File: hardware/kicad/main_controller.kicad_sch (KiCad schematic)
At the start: 24 parts, among them J3 JTAG_10PIN, SW1 RESET, SW2 BOOT, U6 ESP32-S3-MINI-1, Y1 32.768 kHz

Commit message: PCB Layout Update
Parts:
- added D5: ESDA6V1W5, Package_TO_SOT_SMD:SOT-353_SC-70-5, symbol Power_Protection:SP0504BAJT
- added D9 (x2): ESD5651N, Capacitor_SMD:C_0402_1005Metric, symbol Device:D_TVS
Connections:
- net ESP_EN is gone; now on net CHIP_EN: U6.45 (EN)
- net +3V3: now also D9.2 (A2)
- net CELL_EN: now also U6.18 (GPIO14/TOUCH14/ADC2_CH3/FSPIWP/FSPIDQS/SUBSPIWP); no longer U6.30 (GPIO48/SPICLK_N/SUBSPICLK_N_DIFF)
- net CELL_PWRKEY: now also U6.13 (GPIO9/TOUCH9/ADC1_CH8/FSPIHD/SUBSPIHD); no longer U6.27 (GPIO47/SPICLK_P/SUBSPICLK_P_DIFF)
- net CELL_RESET: now also U6.16 (GPIO12/TOUCH12/ADC2_CH1/FSPICLK/FSPIIO6/SUBSPICLK); no longer U6.29 (SPIIO5/GPIO34/FSPICS0/SUBSPICS0)
- net CELL_RXD: now also U6.15 (GPIO11/TOUCH11/ADC2_CH0/FSPID/FSPIIO5/SUBSPID); no longer U6.21 (GPIO17/U1TXD/ADC2_CH6)
- net CELL_STATUS: now also U6.21 (GPIO17/U1TXD/ADC2_CH6); no longer U6.28 (SPIIO4/GPIO33/FSPIHD/SUBSPIHD)
- net CELL_TXD: now also U6.14 (GPIO10/TOUCH10/ADC1_CH9/FSPICS0/FSPIIO4/SUBSPICS0); no longer U6.22 (GPIO18/U1RXD/ADC2_CH7/CLK_OUT3)
- net CHIP_EN: now also D9.2 (A2)
- net FG_INT: now also U6.22 (GPIO18/U1RXD/ADC2_CH7/CLK_OUT3); no longer U6.25 (GPIO21)
- net GND: now also D5.2 (A), D9.1 (A1), D9.1 (A1)
- net GNSS_EN: now also U6.9 (GPIO5/TOUCH5/ADC1_CH4); no longer U6.5 (GPIO1/TOUCH1/ADC1_CH0)
- net GNSS_FO: now also U6.8 (GPIO4/TOUCH4/ADC1_CH3); no longer U6.33 (SPIDQS/GPIO37/FSPIQ/SUBSPIQ)
- net GNSS_RESET: now also U6.5 (GPIO1/TOUCH1/ADC1_CH0); no longer U6.34 (GPIO38/FSPIWP/SUBSPIWP)
- net GNSS_RXD: now also U6.10 (GPIO6/TOUCH6/ADC1_CH5); no longer U6.31 (SPIIO6/GPIO35/FSPID/SUBSPID)
- net GNSS_SDBY: now also U6.6 (GPIO2/TOUCH2/ADC1_CH1); no longer U6.41 (GPIO45)
- net GNSS_TXD: now also U6.11 (GPIO7/TOUCH7/ADC1_CH6); no longer U6.32 (SPIIO7/GPIO36/FSPICLK/SUBSPICLK)
- net GNSS_VBCKP_EN: now also U6.12 (GPIO8/TOUCH8/ADC1_CH7/SUBSPICS1); no longer U6.26 (GPIO26)
- net IMU_INT: now also U6.17 (GPIO13/TOUCH13/ADC2_CH2/FSPIQ/FSPIIO7/SUBSPIQ); no longer U6.6 (GPIO2/TOUCH2/ADC1_CH1)
- net JTAG_TCK: now also D5.3 (K)
- net JTAG_TDI: now also D5.4 (K)
- net JTAG_TDO: now also D5.1 (K)
- net JTAG_TMS: now also D5.5 (K)
- net SCL: now also U6.32 (SPIIO7/GPIO36/FSPICLK/SUBSPICLK); no longer U6.16 (GPIO12/TOUCH12/ADC2_CH1/FSPICLK/FSPIIO6/SUBSPICLK)
- net SDA: now also U6.33 (SPIDQS/GPIO37/FSPIQ/SUBSPIQ); no longer U6.17 (GPIO13/TOUCH13/ADC2_CH2/FSPIQ/FSPIIO7/SUBSPIQ)
- no-connect marks 11 -> 4
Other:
- note added: "ESP32-S3-MINI-N4R2"
- note added: "Octal SPI"
- note added: "internal flash/PSRAM"
- note added: "strapping pin"
- moved on the sheet: C15, C16, J3, R11, R15, R18, R7, R8, R9, TP7, TP8, Y1

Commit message: PCB Layout Update
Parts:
- added D1: Yellow, LED_SMD:LED_0603_1608Metric, symbol Device:LED_Small
- added D1: Green, LED_SMD:LED_0603_1608Metric, symbol Device:LED_Small
- added R5 (x2): 1k, Resistor_SMD:R_0402_1005Metric, symbol Device:R_Small
- added TP7: GPIO38, TestPoint:TestPoint_Pad_D1.0mm, symbol Connector:TestPoint
- added TP7: GPIO45, TestPoint:TestPoint_Pad_D1.0mm, symbol Connector:TestPoint
- added TP7: GPIO35, TestPoint:TestPoint_Pad_D1.0mm, symbol Connector:TestPoint
- added TP7: GPIO03, TestPoint:TestPoint_Pad_D1.0mm, symbol Connector:TestPoint
- added TP7: GPIO21, TestPoint:TestPoint_Pad_D1.0mm, symbol Connector:TestPoint
- added TP7: GPIO34, TestPoint:TestPoint_Pad_D1.0mm, symbol Connector:TestPoint
- added TP7: GPIO33, TestPoint:TestPoint_Pad_D1.0mm, symbol Connector:TestPoint
- added TP7: GPIO46, TestPoint:TestPoint_Pad_D1.0mm, symbol Connector:TestPoint
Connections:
- net GND: now also R5.2, R5.2
- net at U6.25 (GPIO21): now also TP7.1
- net at U6.27 (GPIO47/SPICLK_P/SUBSPICLK_P_DIFF): now also D1.2 (A)
- net at U6.28 (SPIIO4/GPIO33/FSPIHD/SUBSPIHD): now also TP7.1
- net at U6.29 (SPIIO5/GPIO34/FSPICS0/SUBSPICS0): now also TP7.1
- net at U6.30 (GPIO48/SPICLK_N/SUBSPICLK_N_DIFF): now also D1.2 (A)
- net at U6.31 (SPIIO6/GPIO35/FSPID/SUBSPID): now also TP7.1
- net at U6.34 (GPIO38/FSPIWP/SUBSPIWP): now also TP7.1
- net at U6.41 (GPIO45): now also TP7.1
- net at U6.7 (GPIO3/TOUCH3/ADC1_CH2): now also TP7.1
- net BOOT_MODE1: no longer names the net of U6.44 (GPIO46)
- net BOOT_MODE1: now also TP7.1
- new net: D1.1 (K), R5.1 (x2)
- no-connect marks 4 -> 2
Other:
- note added: "ESP32-S3-MINI-N4R2 (Quad SPI)"
- note removed: "ESP32-S3-MINI-N4R2"
- moved on the sheet: R9

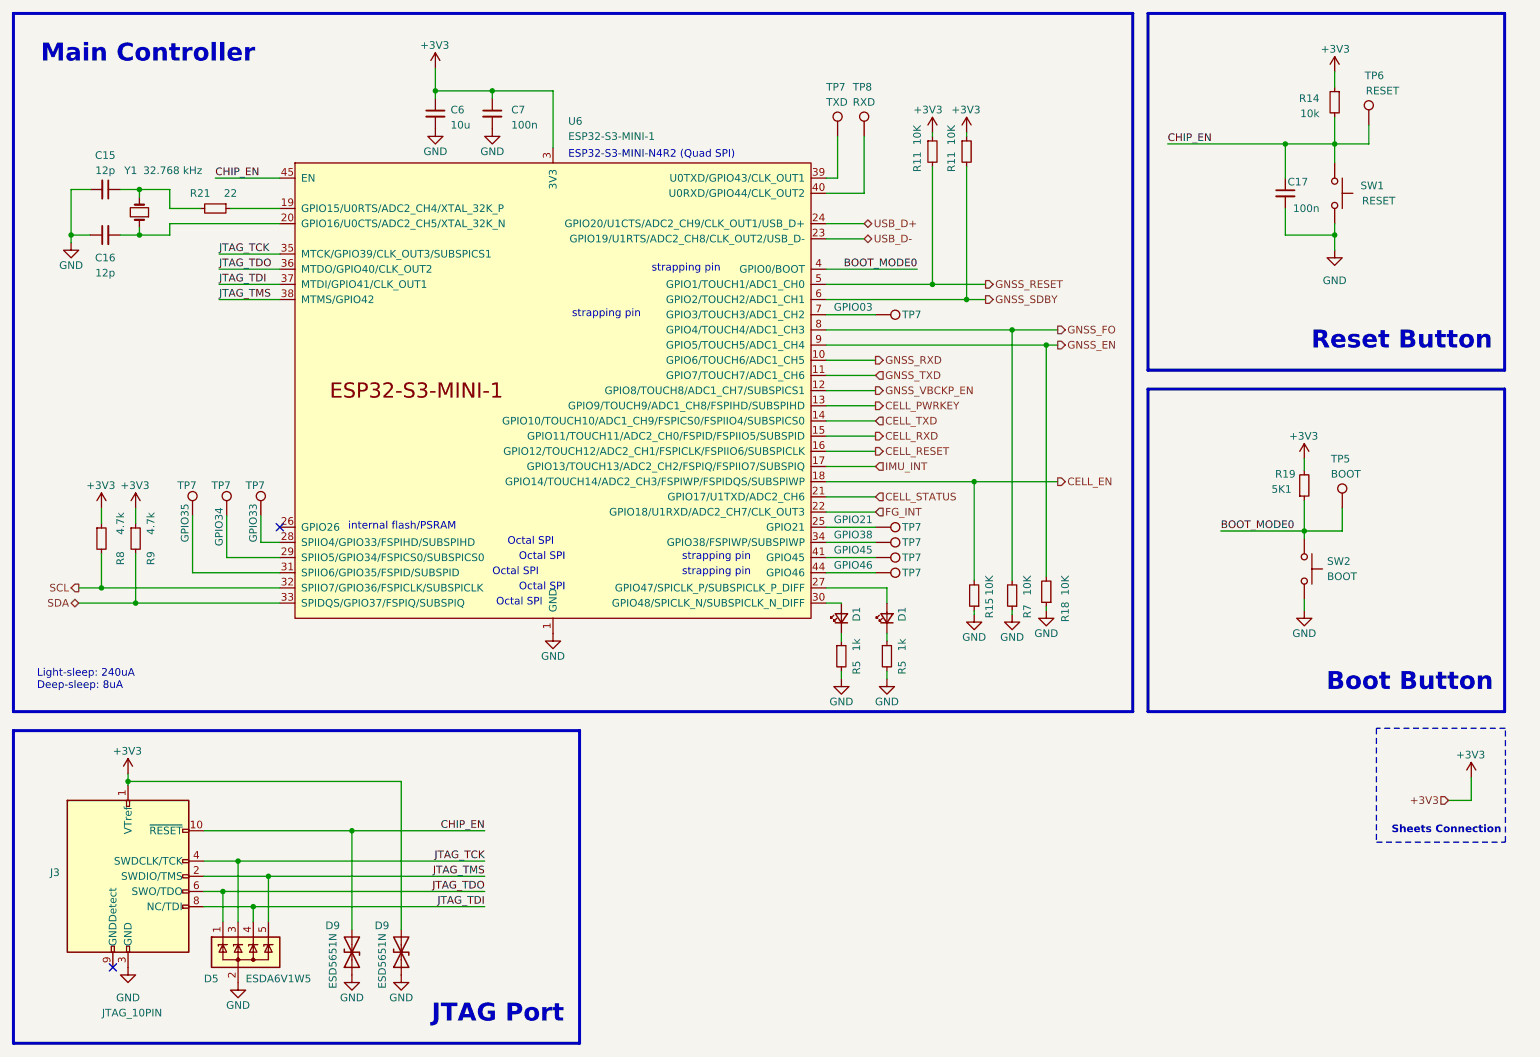
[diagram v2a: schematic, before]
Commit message: update to KiCAD 8 and add cell power regulator
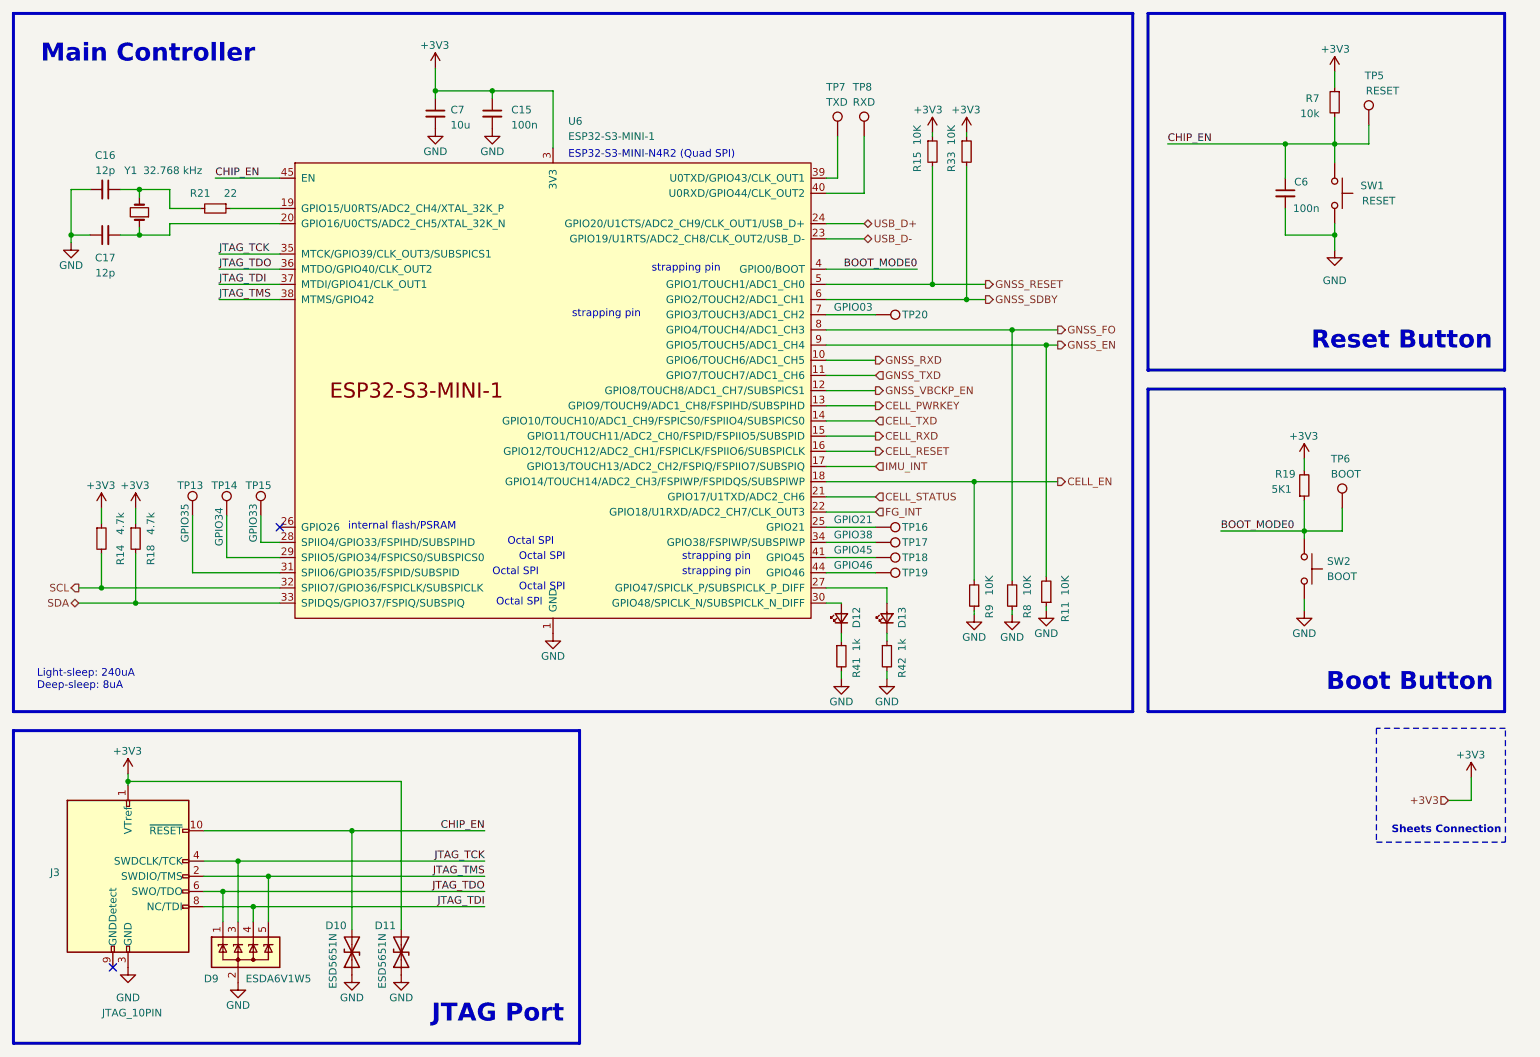
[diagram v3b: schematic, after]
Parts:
- renumbered C7 to C15, C15 to C16, C16 to C17, C17 to C6, C6 to C7, D9 to D10, D9 to D11, D1 to D12, D1 to D13, D5 to D9, R18 to R11, R8 to R14, R11 to R15, R9 to R18, R11 to R33, R5 to R41, R5 to R42, R14 to R7, R7 to R8, R15 to R9, TP7 to TP13, TP7 to TP14, TP7 to TP15, TP7 to TP16, TP7 to TP17, TP7 to TP18, TP7 to TP19, TP7 to TP20, TP6 to TP5, TP5 to TP6

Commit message: move components to use bwlc1a library
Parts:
- SW1, SW2: footprint Button_Switch_SMD:SW_Push_1P1T_NO_CK_KMR2 -> bwlc1a:SW-SMD_L3.9-W3.0-P4.45
- U6: footprint Espressif:ESP32-S3-MINI-1 -> bwlc1a:ESP32-S3-MINI-1; symbol Espressif:ESP32-S3-MINI-1 -> bwlc1a:ESP32-S3-MINI-1
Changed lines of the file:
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@@
 			)
 		)
-		(property "Footprint" "Button_Switch_SMD:SW_Push_1P1T_NO_CK_KMR2"
+		(property "Footprint" "bwlc1a:SW-SMD_L3.9-W3.0-P4.45"
 			(at 245.11 113.03 0)
 			(effects
@@
 	)
 	(symbol
-		(lib_id "Espressif:ESP32-S3-MINI-1")
+		(lib_id "bwlc1a:ESP32-S3-MINI-1")
 		(at 114.3 83.185 0)
 		(unit 1)
@@
 			)
 		)
-		(property "Footprint" "Espressif:ESP32-S3-MINI-1"
+		(property "Footprint" "bwlc1a:ESP32-S3-MINI-1"
 			(at 114.3 139.065 0)
 			(effects
@@
 			)
 		)
-		(property "Description" "SMD WiFi Modules ROHS"
+		(property "Description" "Smallsized module supporting 2.4 GHz WiFi (802.11 b/g/n) and Bluetooth ® 5 (LE) Built around ESP32S3 series of SoCs, Xtensa ® dualcore 32bit LX7 microprocessor Flash up to 8 MB, optional 2 MB PSRAM in chip package 39 GPIOs, rich set of peripherals Onboard PCB antenna or external antenna connector"
 			(at 114.3 83.185 0)
 			(effects
@@
 			)
 		)
+		(property "Manufacturer" ""
+			(at 114.3 83.185 0)
+			(effects
+				(font
+					(size 1.27 1.27)
+				)
+				(hide yes)
+			)
+		)
+		(property "Manufacturer Part Number" ""
+			(at 114.3 83.185 0)
+			(effects
+				(font
+					(size 1.27 1.27)
+				)
+				(hide yes)
+			)
+		)
 		(pin "1"
 		)
@@
 			)
 		)
-		(property "Footprint" "Button_Switch_SMD:SW_Push_1P1T_NO_CK_KMR2"
+		(property "Footprint" "bwlc1a:SW-SMD_L3.9-W3.0-P4.45"
 			(at 250.19 50.165 0)
 			(effects
@@
 			(at 245.11 50.165 0)
 			(effects
+				(font
+					(size 1.27 1.27)
+				)
+				(hide yes)
+			)
+		)
+		(property "Manufacturer" ""
+			(at 245.11 50.165 0)
+			(effects
+				(font
+					(size 1.27 1.27)
+				)
+				(hide yes)
+			)
+		)
+		(property "Manufacturer Part Number" ""
+			(at 245.11 50.165 0)
+			(effects

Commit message: update bill of materials
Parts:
- C15, C6: Id 3 -> (none); Manufacture Samsung Electro-Mechanics -> (none); Manufacture Part Number CL05B104KO5NNNC -> (none); Manufacturer (none) -> Samsung Electro-Mechanics; Manufacturer Part Number (none) -> CL05B104KO5NNNC; Type SMD -> (none)
- C16, C17: Id 5 -> (none); Manufacture FH (Guangdong Fenghua Advanced Tech) -> (none); Manufacture Part Number 0402CG120J500NT -> (none); Manufacturer (none) -> FH (Guangdong Fenghua Advanced Tech); Manufacturer Part Number (none) -> 0402CG120J500NT; Type SMD -> (none)
- C7: Id 1 -> (none); Manufacture Samsung Electro-Mechanics -> (none); Manufacture Part Number CL10A106KP8NNNC -> (none); Manufacturer (none) -> Samsung Electro-Mechanics; Manufacturer Part Number (none) -> CL10A106KP8NNNC; Type SMD -> (none)
- D10, D11: Distributor (none) -> LCSC; Distributor Part Number (none) -> C5173251; Manufacturer (none) -> Leiditech; Manufacturer Part Number (none) -> ESD5651N
- D12: value Yellow -> LTST-C191KGKT; Distributor Link https://www.lcsc.com/product-detail/Light-Emitting-Diodes-LED_EKINGLUX-E6C0603SEAC1UDA_C375450.html -> https://www.lcsc.com/product-detail/Light-Emitting-Diodes-LED_Lite-On-LTST-C191KGKT_C125098.html; Distributor Part Number C375450 -> C125098; Id 17 -> (none); Manufacture EKINGLUX -> (none); Manufacture Part Number E6C0603SEAC1UDA -> (none); Manufacturer (none) -> Lite-On; Manufacturer Part Number (none) -> LTST-C191KGKT; Type SMD -> (none)
- D13: value Green -> LTST-C191KRKT; Distributor Link https://www.lcsc.com/product-detail/Light-Emitting-Diodes-LED_EKINGLUX-E6C0603SEAC1UDA_C375450.html -> https://www.lcsc.com/product-detail/Light-Emitting-Diodes-LED_Lite-On-LTST-C191KRKT_C125099.html; Distributor Part Number C375450 -> C125099; Id 17 -> (none); Manufacture EKINGLUX -> (none); Manufacture Part Number E6C0603SEAC1UDA -> (none); Manufacturer (none) -> Lite-On; Manufacturer Part Number (none) -> LTST-C191KRKT; Type SMD -> (none)
- D9: Id 20 -> (none); Manufacture TECH PUBLIC -> (none); Manufacture Part Number ESDA6V1W5-TP -> (none); Manufacturer (none) -> TECH PUBLIC; Manufacturer Part Number (none) -> ESDA6V1W5-TP; Type SMD -> (none)
- J3: value JTAG_10PIN -> Tag-Connect_TC2050-IDC-NL; Distributor - -> (none); Distributor Link - -> (none); Distributor Part Number - -> (none); Id 26 -> (none); Manufacture - -> (none); Manufacture Part Number - -> (none); Type SMD -> (none)
- R11, R15, R33, R8, R9: Distributor Link https://www.lcsc.com/product-detail/Chip-Resistor-Surface-Mount_UNI-ROYAL-Uniroyal-Elec-0402WGF1004TCE_C26083.html -> https://www.lcsc.com/product-detail/Chip-Resistor-Surface-Mount_UNI-ROYAL-Uniroyal-Elec-0402WGF1002TCE_C25744.html; Distributor Part Number C26083 -> C25744; Id 42 -> (none); Manufacture UNI-ROYAL(Uniroyal Elec) -> (none); Manufacture Part Number 0402WGF1004TCE -> (none); Manufacturer (none) -> UNI-ROYAL(Uniroyal Elec); Manufacturer Part Number (none) -> 0402WGF1002TCE; Type SMD -> (none)
- R14, R18: Id 39 -> (none); Manufacture UNI-ROYAL(Uniroyal Elec) -> (none); Manufacture Part Number 0402WGJ0472TCE -> (none); Manufacturer (none) -> UNI-ROYAL(Uniroyal Elec); Manufacturer Part Number (none) -> 0402WGJ0472TCE; Type SMD -> (none)
- R19: Part Description Resistor 62.5mW ±1% 5.1kΩ -> (none)
- R21: Part Description Resistor 62.5mW ±1% 22Ω -> (none)
- R41, R42: Id 37 -> (none); Manufacture UNI-ROYAL(Uniroyal Elec) -> (none); Manufacture Part Number 0402WGJ0102TCE -> (none); Manufacturer (none) -> UNI-ROYAL(Uniroyal Elec); Manufacturer Part Number (none) -> 0402WGJ0102TCE; Type SMD -> (none)
- R7: Id 40 -> (none); Manufacture UNI-ROYAL(Uniroyal Elec) -> (none); Manufacture Part Number 0402WGF1002TCE -> (none); Manufacturer (none) -> UNI-ROYAL(Uniroyal Elec); Manufacturer Part Number (none) -> 0402WGF1002TCE; Type SMD -> (none)
- SW1: Id 46 -> (none); Manufacture C&K -> (none); Manufacture Part Number KMR233GLFG -> (none); Manufacturer (none) -> C&K; Manufacturer Part Number (none) -> KMR233GLFG; Type SMD -> (none)
- SW2: Id 29 -> (none); Manufacture C&K -> (none); Manufacture Part Number KMR233GLFG -> (none); Manufacturer (none) -> C&K; Manufacturer Part Number (none) -> KMR233GLFG; Type SMD -> (none)
- U6: Id 56 -> (none); Manufacture Espressif Systems -> (none); Manufacture Part Number ESP32-S3-MINI-1-N4R2 -> (none); Manufacturer (none) -> Espressif Systems; Manufacturer Part Number (none) -> ESP32-S3-MINI-1-N4R2; Type SMD -> (none)
- Y1: Id 60 -> (none); Manufacture Seiko Epson -> (none); Manufacture Part Number Q13FC1350000400 -> (none); Manufacturer (none) -> Seiko Epson; Manufacturer Part Number (none) -> Q13FC1350000400; Type SMD -> (none)
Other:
- note added: "Green"
- note added: "Red"

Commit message: update bill of materials
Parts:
- D10, D11: footprint Capacitor_SMD:C_0402_1005Metric -> Diode_SMD:D_SOD-882
- R11, R15, R33, R8, R9: value 10K -> 10k
- R14, R18: value 4.7k -> 4k7
- R19: value 5K1 -> 5k1
- R21: Distributor Link https://www.lcsc.com/product-detail/Chip-span-style-backgro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 -> https://www.lcsc.com/product-detail/Chip-Resistor-Surface-M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
- SW1: value RESET -> KMR233GLFG
- SW2: value BOOT -> KMR233GLFG
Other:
- note added: "BOOT"
- note added: "RESET"
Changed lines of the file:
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@@
 		)
 	)
+	(text "RESET"
+		(exclude_from_sim no)
+		(at 258.064 49.276 0)
+		(effects
+			(font
+				(size 1.27 1.27)
+			)
+		)
+	)
 	(text "Octal SPI"
 		(exclude_from_sim no)
@@
 		)
 	)
+	(text "BOOT"
+		(exclude_from_sim no)
+		(at 236.982 113.284 90)
+		(effects
+			(font
+				(size 1.27 1.27)
+			)
+		)
+	)
 	(text "strapping pin"
 		(exclude_from_sim no)
@@
 			)
 		)
-		(property "Value" "BOOT"
+		(property "Value" "KMR233GLFG"
 			(at 243.84 114.3 90)
 			(effects
@@
 			)
 		)
-		(property "Value" "10K"
+		(property "Value" "10k"
 			(at 193.675 117.475 90)
 			(effects
@@
 			)
 		)
-		(property "Value" "10K"
+		(property "Value" "10k"
 			(at 180.975 38.735 90)
 			(effects
@@
 			)
 		)
-		(property "Value" "4.7k"
+		(property "Value" "4k7"
 			(at 46.99 107.315 90)
 			(effects
@@
 			)
 		)
-		(property "Datasheet" "https://datasheet.lcsc.com/lcsc/2205311900_UNI-ROYAL-Uniroyal-Elec-0402WGF220JTCE_C25092.pdf"
+		(property "Datasheet" "https://www.lcsc.com/datasheet/lcsc_datasheet_2205311900_UNI-ROYAL-Uniroyal-Elec-0402WGF220JTCE_C25092.pdf"
 			(at 57.785 52.705 0)
 			(effects
@@
 			)
 		)
-		(property "Description" "62.5mW Thick Film Resistors 50V ±1% ±100ppm/℃ 22Ω 0402 Chip Resistor - Surface Mount ROHS"
+		(property "Description" "62.5mW Thick Film Resistors ±1% ±100ppm/℃ 22Ω 0402 Chip Resistor - Surface Mount ROHS"
 			(at 57.785 52.705 0)
 			(effects
@@
 			)
 		)
-		(property "Distributor Link" "https://www.lcsc.com/product-detail/Chip-span-style-background-color-ff0-Resistor-span-Surface-Mount_UNI-ROYAL-Uniroyal-Elec-0402WGF220JTCE_C25092.html"
+		(property "Distributor Link" "https://www.lcsc.com/product-detail/Chip-Resistor-Surface-Mount_UNI-ROYAL-Uniroyal-Elec-0402WGF220JTCE_C25092.html"
 			(at 57.785 52.705 0)
 			(effects
@@
 			)
 		)
-		(property "Footprint" "Capacitor_SMD:C_0402_1005Metric"
+		(property "Footprint" "Diode_SMD:D_SOD-882"
 			(at 88.9 177.165 0)
 			(effects
@@
 			)
 		)
-		(property "Value" "RESET"
-			(at 255.27 51.435 90)
+		(property "Value" "KMR233GLFG"
+			(at 261.874 51.562 90)
 			(effects
 				(font
@@
 			)
 		)
-		(property "Value" "10K"
+		(property "Value" "10k"
 			(at 175.26 38.735 90)
 			(effects
@@
 			)
 		)
-		(property "Description" "SOT-353 Electrostatic and Surge Protection (TVS/ESD) ROHS"
+		(property "Description" "SOT-323-5 ESD Protection Devices ROHS"
 			(at 61.595 177.165 0)
 			(effects
@@
 			)
 		)
-		(property "Value" "4.7k"
+		(property "Value" "4k7"
 			(at 41.91 107.315 90)
 			(effects
@@
 			)
 		)
-		(property "Value" "10K"
+		(property "Value" "10k"
 			(at 200.025 117.475 90)
 			(effects
@@
 			)
 		)
-		(property "Footprint" "Capacitor_SMD:C_0402_1005Metric"
+		(property "Footprint" "Diode_SMD:D_SOD-882"
 			(at 80.645 177.165 0)
 			(effects
@@
 			)
 		)
-		(property "Value" "5K1"
+		(property "Value" "5k1"
 			(at 236.22 99.695 0)
 			(effects
@@
 			)
 		)
-		(property "Datasheet" "https://datasheet.lcsc.com/lcsc/2206010045_UNI-ROYAL-Uniroyal-Elec-0402WGF5101TCE_C25905.pdf"
+		(property "Datasheet" "https://www.lcsc.com/datasheet/lcsc_datasheet_2206010045_UNI-ROYAL-Uniroyal-Elec-0402WGF5101TCE_C25905.pdf"
 			(at 240.03 99.06 0)
 			(effects
@@
 			)
 		)
-		(property "Description" "62.5mW Thick Film Resistors 50V ±100ppm/℃ ±1% 5.1kΩ 0402 Chip Resistor - Surface Mount ROHS"
+		(property "Description" "62.5mW Thick Film Resistors ±100ppm/℃ ±1% 5.1kΩ 0402 Chip Resistor - Surface Mount ROHS"
 			(at 240.03 99.06 0)
 			(effects
@@
 			)
 		)
-		(property "Value" "10K"
+		(property "Value" "10k"
 			(at 187.325 117.475 90)
 			(effects
@@
 			)
 		)
-		(property "Description" " 62.5mW Thick Film Resistors 50V ±100ppm/℃ ±1% 10kΩ 0402 Chip Resistor - Surface Mount ROHS"
+		(property "Description" "62.5mW Thick Film Resistors 50V ±100ppm/℃ ±1% 10kΩ 0402 Chip Resistor - Surface Mount ROHS"
 			(at 184.785 117.475 0)
 			(effects

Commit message: add page info
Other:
- company: (none) -> Teapot Laboratories
- title: (none) -> Main Controller
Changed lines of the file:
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@@
 	(generator_version "8.0")
 	(paper "A4")
+	(title_block
+		(title "Main Controller")
+		(date "2024-05-17")
+		(rev "1")
+		(company "Teapot Laboratories")
+	)
 	(junction
 		(at 184.785 98.425)
